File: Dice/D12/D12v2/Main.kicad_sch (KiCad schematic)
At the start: 30 parts, among them J1 Conn_01x14, J2 Conn_01x11, U1 N52810_QFN32, U2 KXTJ3-1057, X101 DNP, X102 DNP, Y1 32MHz 40ppm

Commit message: More Cleanup of Dice Boards
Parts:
- removed X101, X102: DNP, Capacitor_SMD:C_0402_1005Metric, symbol Device:R_Small
- C1, C10, C2, C3, C4, C5, C7: footprint Pixels-dice:C_0402_1005Metric -> Capacitor_SMD:C_0402_1005Metric
- C11, C8: footprint Pixels-dice:0402_RF -> Capacitor_SMD:C_0402_1005Metric
- L5: footprint Pixels-dice:0402_RF -> Inductor_SMD:L_0402_1005Metric
- R10, R12, R16: footprint Pixels-dice:R_0402_1005Metric -> Resistor_SMD:R_0402_1005Metric
- R9: value 100k 1% -> 180k 1%; footprint Pixels-dice:R_0402_1005Metric -> Resistor_SMD:R_0402_1005Metric; Manufacturer Vishay -> (none); Manufacturer Part Number CRCW0402100KFKEDC -> (none)
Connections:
- net LED_RETURN: now reaches U1.8 (P0.10)
- net LEDs/LED_RETURN: no longer names the net of U1.7 (P0.09)
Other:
- note removed: "0402 Components used as registration pin for counterweight."

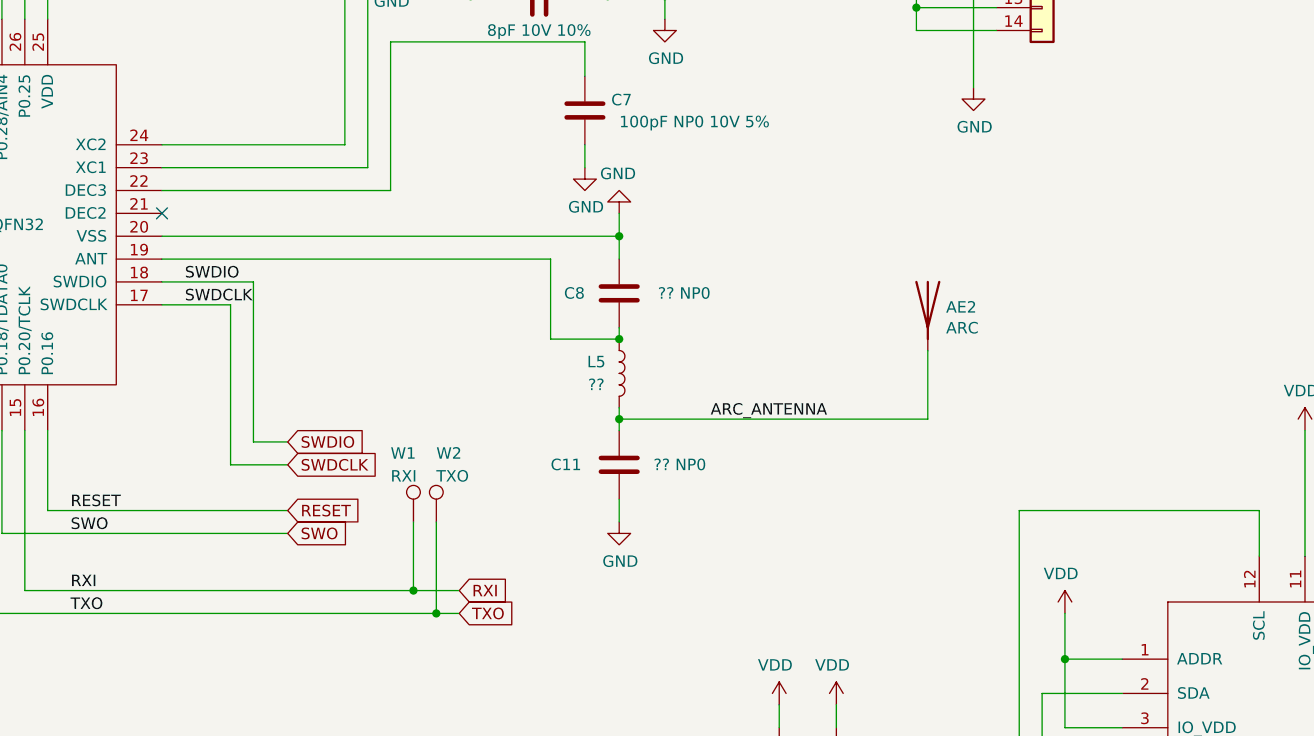
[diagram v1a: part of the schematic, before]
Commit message: Updating D8 and D10 boards, new antenna, etc...
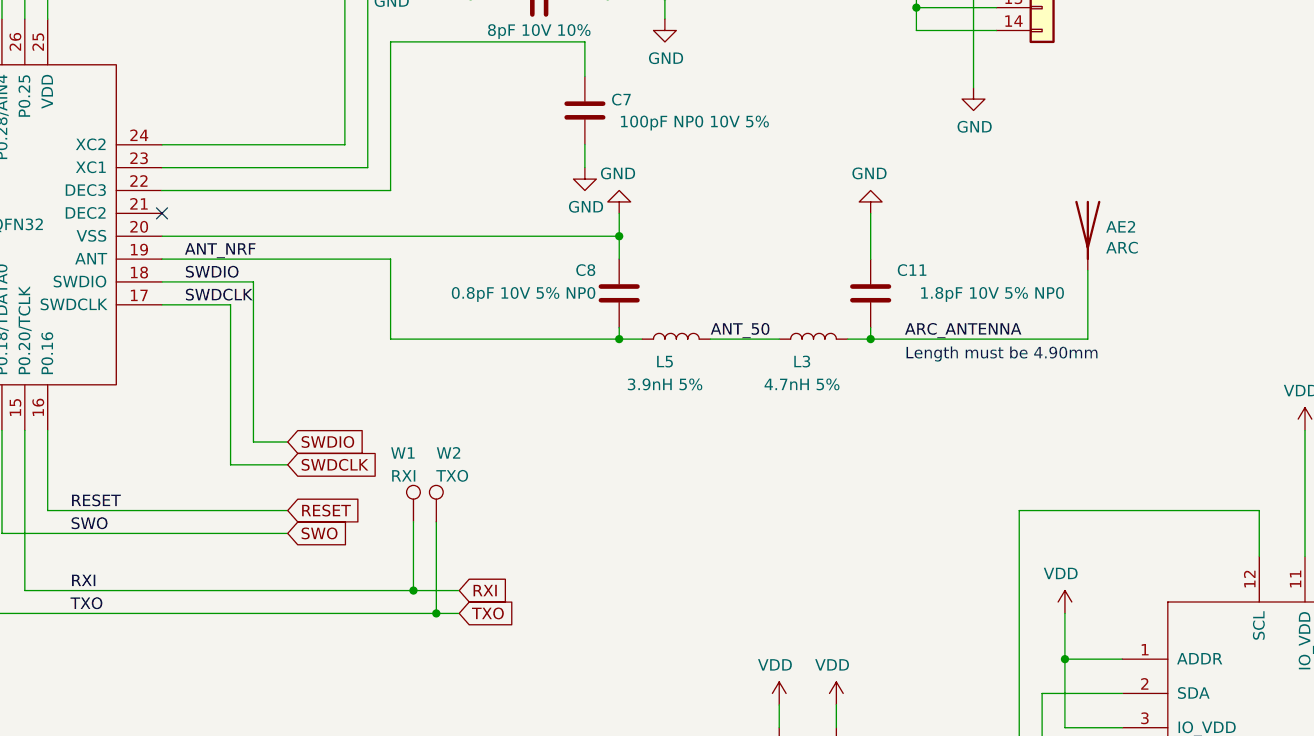
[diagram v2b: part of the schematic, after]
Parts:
- added L3: 4.7nH 5%, Pixels-dice:0402_RF, symbol Device:L
- AE2: Generic OK (none) -> N/A; Manufacturer (none) -> AEM Antennas
- C11: value ?? NP0 -> 1.8pF 10V 5% NP0; footprint Capacitor_SMD:C_0402_1005Metric -> Pixels-dice:0402_RF; Manufacturer (none) -> Murata; Manufacturer Part Number (none) -> GCM1555C1H1R8BA16D; Pixels Part Number (none) -> SMD-C004
- C2, C5: Manufacturer (none) -> Murata; Manufacturer Part Number (none) -> GRM1555C2A8R0DA01D
- C8: value ?? NP0 -> 0.8pF 10V 5% NP0; footprint Capacitor_SMD:C_0402_1005Metric -> Pixels-dice:0402_RF; Manufacturer (none) -> Murata; Manufacturer Part Number (none) -> GCM1555C1HR80BA16D
- J1, J2, W1, W2, W5, W7, W8, W9: Generic OK (none) -> N/A
- L5: value ?? -> 3.9nH 5%; footprint Inductor_SMD:L_0402_1005Metric -> Pixels-dice:0402_RF; Manufacturer (none) -> Murata; Manufacturer Part Number (none) -> LQG15HS3N9B02D
- R9: Manufacturer (none) -> Yageo; Manufacturer Part Number (none) -> RC0402FR-13180KL
- U2: Generic OK (none) -> NO
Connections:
- net ARC_ANTENNA: now also L3.2; no longer L5.2
- net ANT_NRF: now reaches C8.1, L5.1, U1.19 (ANT)
- new net ANT_50: L3.1, L5.2
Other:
- note added: "Length must be 4.90mm"

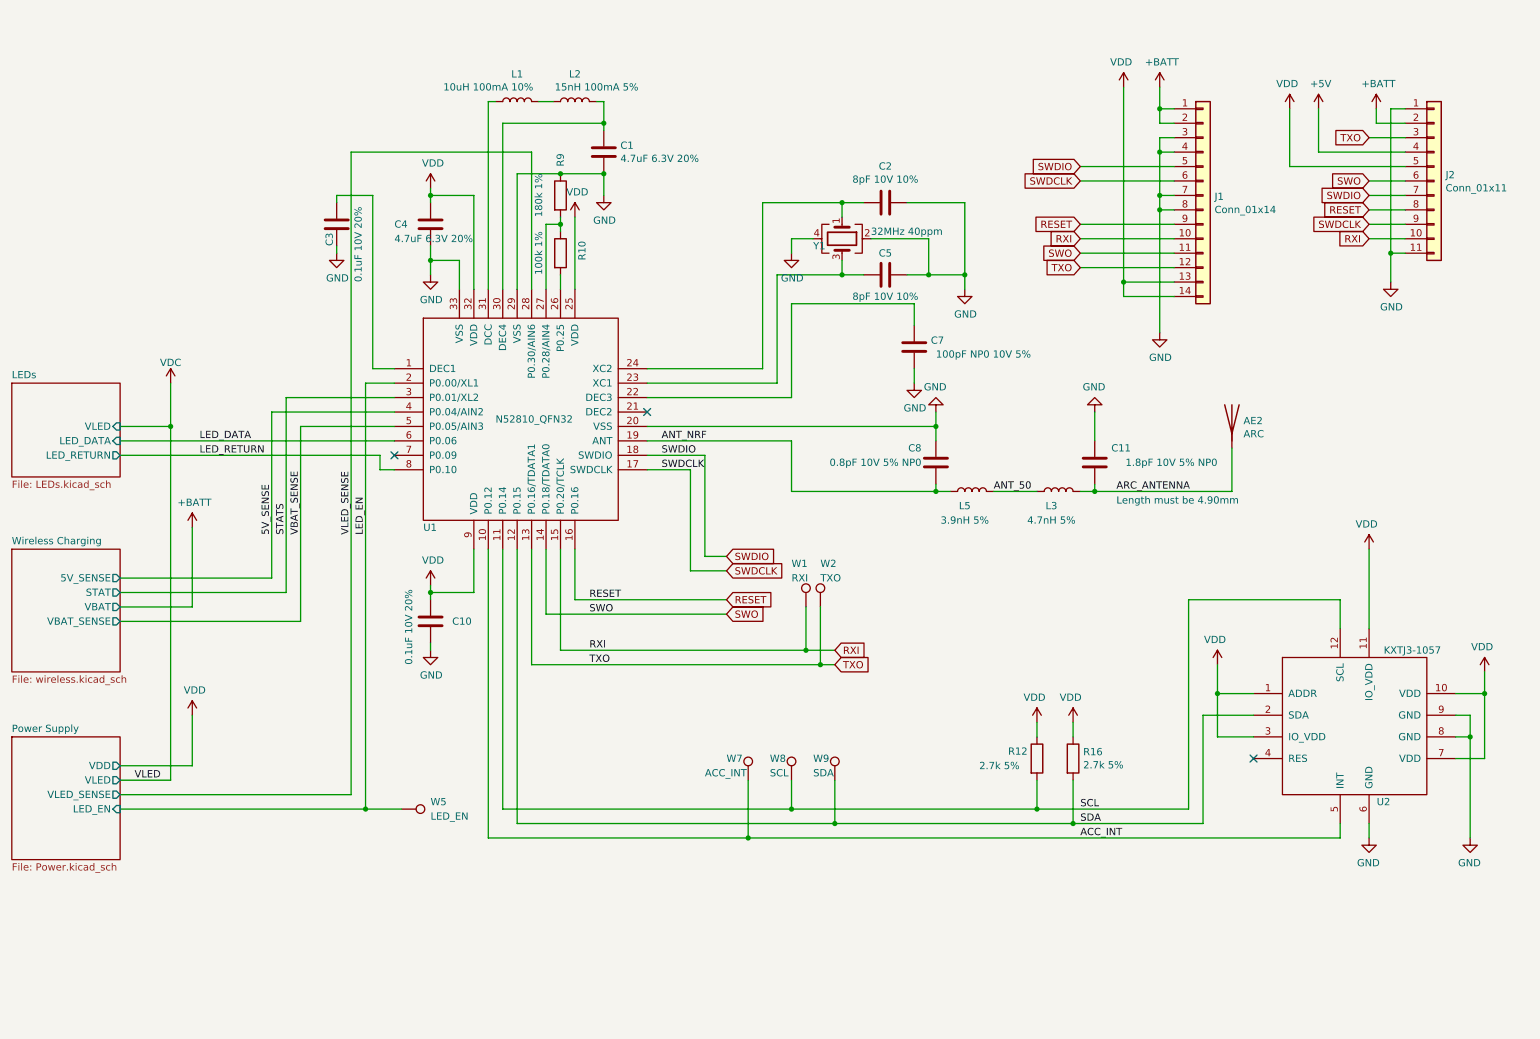
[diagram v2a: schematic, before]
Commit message: Updated all remaining boards to match D20V15 (D6, PD6, D8, D10 and D12)
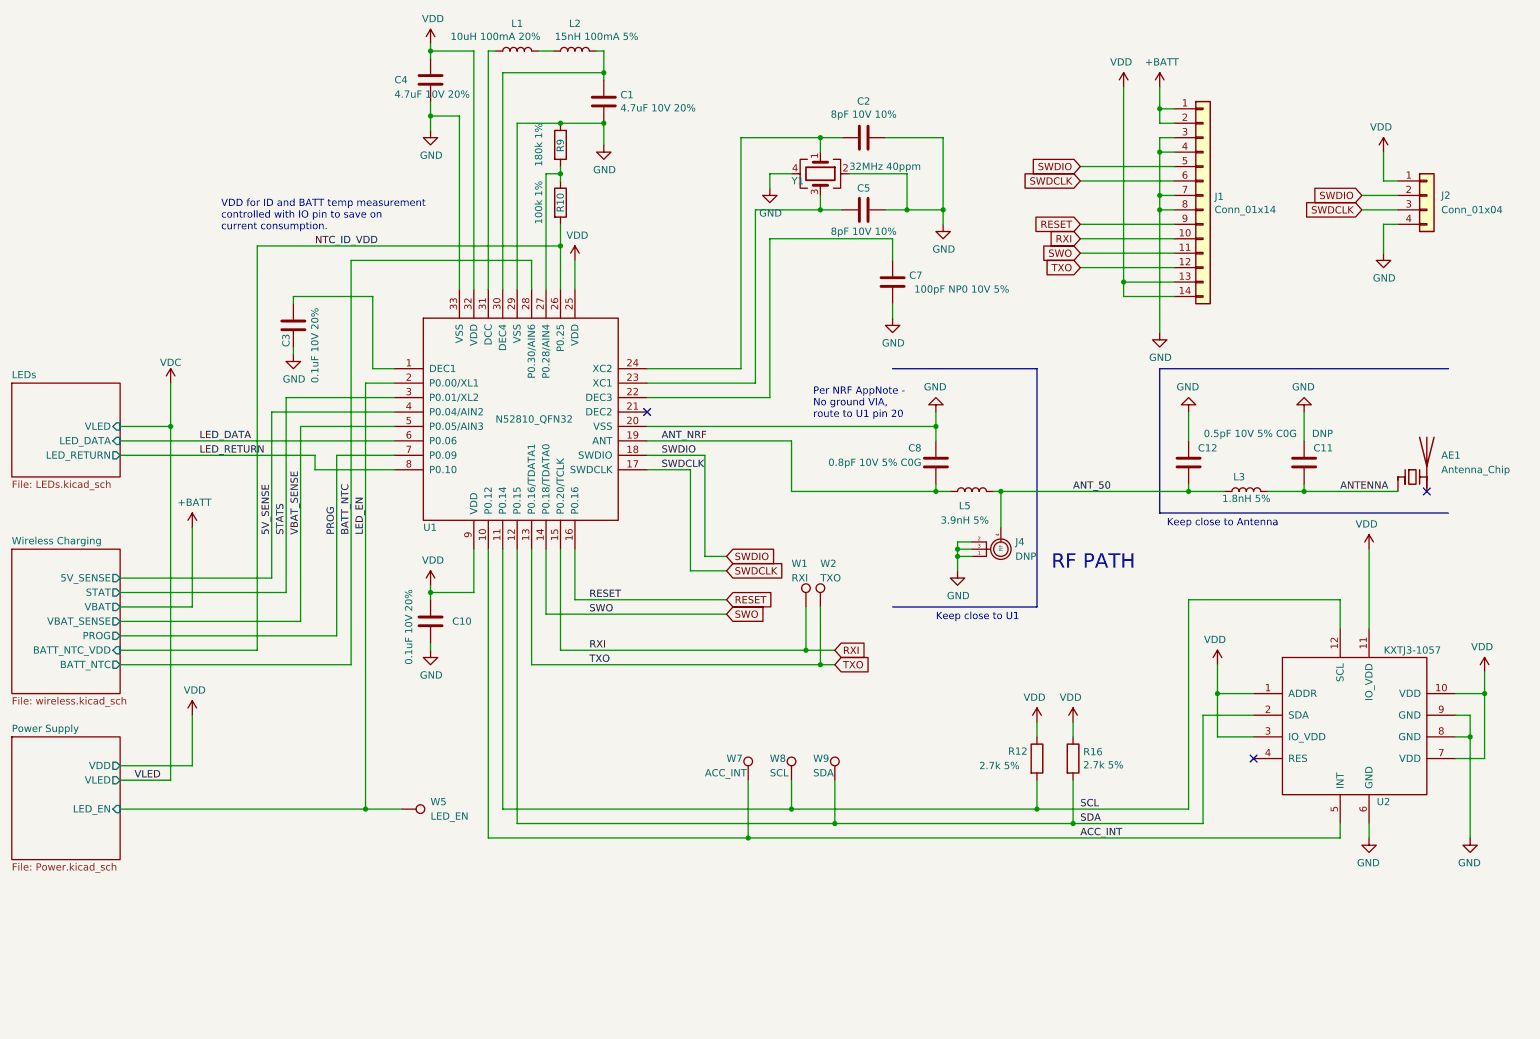
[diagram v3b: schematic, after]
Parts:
- removed AE2: ARC, Pixels-dice:ARC_Antenna, symbol Device:Antenna
- removed J2: Conn_01x11, Pixels-dice:FPC-POGO-11, symbol Connector_Generic:Conn_01x11
- added AE1: Antenna_Chip, Pixels-dice:CHIP_ANT, symbol Device:Antenna_Chip
- added C12: 0.5pF 10V 5% C0G, Pixels-dice:0402_RF, symbol Device:C
- added J2: Conn_01x04, Pixels-dice:FPC-POGO-4, symbol Connector_Generic:Conn_01x04
- added J4: DNP, RFFrontEnd:MFH3.RECE.20369.001E.01, symbol Pixels-dice:W.FL
- C1, C4: value 4.7uF 6.3V 20% -> 4.7uF 10V 20%; footprint Capacitor_SMD:C_0402_1005Metric -> Pixels-dice:C_0402_1005Metric; Manufacturer Part Number GRM155R60J475ME87D -> GRM155R61A475MEAAJ
- C10, C3: footprint Capacitor_SMD:C_0402_1005Metric -> Pixels-dice:C_0402_1005Metric
- C11: value 1.8pF 10V 5% NP0 -> DNP; Manufacturer Murata -> (none); Manufacturer Part Number GCM1555C1H1R8BA16D -> (none); Pixels Part Number SMD-C004 -> (none)
- C2, C5: footprint Capacitor_SMD:C_0402_1005Metric -> Pixels-dice:C_0402_1005Metric; Manufacturer Part Number GRM1555C2A8R0DA01D -> GRT1555C2A8R0DA02
- C7: footprint Capacitor_SMD:C_0402_1005Metric -> Pixels-dice:C_0402_1005Metric; Manufacturer Kemet -> Murata; Manufacturer Part Number C0402C101J5GAC7411 -> GCM1555C1H101JA16J
- C8: value 0.8pF 10V 5% NP0 -> 0.8pF 10V 5% C0G; Manufacturer Part Number GCM1555C1HR80BA16D -> GJM1555C1HR80BB01
- L1: value 10uH 100mA 10% -> 10uH 100mA 20%; Manufacturer Taiyo Yuden -> Murata; Manufacturer Part Number LBR2012T100K -> LQM21FN100M80L
- L2: Manufacturer Taiyo Yuden -> Murata; Manufacturer Part Number HK100515NJ-T -> LQG15HS15NJ02D
- L3: value 4.7nH 5% -> 1.8nH 5%; Manufacturer Part Number LQG15HN4N7S02D -> LQG15HZ1N8C02D
- R10: footprint Resistor_SMD:R_0402_1005Metric -> Pixels-dice:R_0402_1005Metric; Manufacturer Vishay -> UNI-ROYAL(Uniroyal Elec); Manufacturer Part Number CRCW0402100KFKEDC -> 0402WGF1003TCE
- R12, R16: footprint Resistor_SMD:R_0402_1005Metric -> Pixels-dice:R_0402_1005Metric; Manufacturer Yageo -> UNI-ROYAL(Uniroyal Elec); Manufacturer Part Number RC0402JR-072K7L -> 0402WGJ0272TCE
- R9: Manufacturer Yageo -> UNI-ROYAL(Uniroyal Elec); Manufacturer Part Number RC0402FR-13180KL -> 0402WGF1803TCE
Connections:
- net ANT_50: now also C12.1, J4.4 (RF)
- net GND: now also C12.2, J2.4 (Pin_4), J4.1, J4.2, J4.3
- net SWDCLK: now also J2.3 (Pin_3)
- net SWDIO: now also J2.2 (Pin_2)
- net VDD: now also J2.1 (Pin_1)
- net NTC_ID_VDD: now reaches R10.2, U1.26 (P0.25)
- net PROG: now reaches U1.7 (P0.09)
- net ARC_ANTENNA renamed ANTENNA
- net ANTENNA: now also AE1.1 (FEED)
- net VLED_SENSE renamed BATT_NTC
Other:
- sheet Power Supply ports: added none; removed VLED_SENSE
- sheet Wireless Charging ports: added BATT_NTC, BATT_NTC_VDD, PROG; removed none
- note added: "Keep close to Antenna"
- note added: "Keep close to U1"
- note added: "Per NRF AppNote - No ground VIA, route to U1 pin 20"
- note added: "RF PATH"
- note added: "VDD for ID and BATT temp measurement controlled with IO pin to save on current consumption."
- note removed: "Length must be 4.90mm"
- title: Pixels D20 Schematic, Main -> Pixels D12 Schematic, Main
- moved on the sheet: C1, C2, C3, C4, C5, C7, L1, L2, R10, R9, Y1
